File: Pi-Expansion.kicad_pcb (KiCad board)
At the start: 2 copper layers, 56 x 65 mm, 130 parts, among them J1 RPi_GPIO, J2 MMCX_H, J3 PINHEADER_2X2_SMD, P1 BATT, Q1 Q_NPN_BCE, U1 A2200-A, U2 SPX2920U-5.0

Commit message: made minor mods to power supply including moving reverse protection diode from negitive side to positive side to reduce voltage drop.
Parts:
- F1: value FUSE -> POLYFUSE
- U2: value SPX2920U-5.0 -> Racom R-78B5.0-1.5L
- moved D1 14.3 mm to (93.5, 128.5)
- moved D2 4.40 mm to (96.0, 128.5)
- moved U2 3.22 mm to (94.8, 125.2)
- moved F1 3.20 mm to (104.5, 120.5), turned to 0 degrees
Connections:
- D1 pad A: GND -> Net-(D1-PadA)
- F1 pad 1: Net-(F1-Pad1) -> GND
- P1 pad 1: Net-(D1-PadK) -> Net-(F1-Pad2)
- P1 pad 2: Net-(F1-Pad1) -> Net-(D1-PadA)
- U1 pad 23: GND -> (no net)
- U1 pad 24: GND -> (no net)
- U1 pad 25: GND -> (no net)
- U1 pad 26: GND -> (no net)
- U1 pad 27: GND -> (no net)
- U1 pad 29: GND -> (no net)
- U1 pad 30: GND -> (no net)
- U1 pad 31: GND -> (no net)
- U1 pad 32: GND -> (no net)
- U2 pad 1: Net-(F1-Pad2) -> Net-(D1-PadK)
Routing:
- net GND: track 78.3 -> 46.7 mm, vias 1 -> 3
- net Net-(D1-PadA): track 0.00 -> 12.9 mm
- net Net-(F1-Pad1): track 9.34 -> 0.00 mm
- net +5V: track 131.6 -> 135.3 mm
- net Net-(D1-PadK): track 2.52 -> 5.43 mm

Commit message: minor tweaks to in fill
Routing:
- net Net-(J2-Pad2): track 19.7 -> 1.47 mm
- added copper zone on F.Cu, net Net-(J2-Pad2)
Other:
- board text added: "2K2"
- board text removed: "GPLv3"
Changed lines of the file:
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@@
     (area 67.819999 72.349999 124.320001 137.850001)
     (thickness 1.6)
-    (drawings 26)
-    (tracks 331)
+    (drawings 25)
+    (tracks 321)
     (zones 0)
     (modules 130)
@@
     (effects (font (size 1 1) (thickness 0.25)))
   )
-  (gr_text 10K (at 80.75 122.25) (layer F.SilkS)
+  (gr_text 2K2 (at 80.75 122.25) (layer F.SilkS)
     (effects (font (size 1 1) (thickness 0.25)))
   )
@@
     (effects (font (size 1.5 1.5) (thickness 0.3)))
   )
-  (gr_text GPLv3 (at 112.25 83.75 90) (layer F.SilkS)
-    (effects (font (size 1.5 1.5) (thickness 0.3)))
-  )
   (gr_text 3.3v (at 93.7 108.9) (layer F.SilkS)
     (effects (font (size 1.5 1.5) (thickness 0.3)))
@@
   (gr_arc (start 71.57 76.1) (end 68.07 76.1) (angle 90) (layer Edge.Cuts) (width 0.5))
   (gr_arc (start 71.57 134.1) (end 71.57 137.6) (angle 90) (layer Edge.Cuts) (width 0.5))
-  (segment (start 103.75 125) (end 103.75 124.89808) (width 0.25) (layer F.Cu) (net 0))
   (segment (start 81.89 105.5) (end 76.25 105.5) (width 0.5) (layer B.Cu) (net 1))
   (segment (start 76.25 105.5) (end 72.84 108.91) (width 0.5) (layer B.Cu) (net 1))
@@
   (segment (start 79 97.42) (end 79 99.96) (width 0.5) (layer B.Cu) (net 9))
   (segment (start 79 99.96) (end 79 102.5) (width 0.5) (layer B.Cu) (net 9))
-  (segment (start 112.24 132.33) (end 112.24 130.76) (width 0.25) (layer F.Cu) (net 10) (status 10))
-  (segment (start 112.75 128.25) (end 111.95 127.45) (width 0.25) (layer F.Cu) (net 10) (status 20))
-  (segment (start 112.75 130.25) (end 112.75 128.25) (width 0.25) (layer F.Cu) (net 10))
-  (segment (start 112.24 130.76) (end 112.75 130.25) (width 0.25) (layer F.Cu) (net 10))
   (segment (start 111.95 127.45) (end 110.55 127.45) (width 0.25) (layer F.Cu) (net 10) (status 30))
-  (segment (start 110.55 127.45) (end 109.75 128.25) (width 0.25) (layer F.Cu) (net 10) (status 10))
-  (segment (start 109.75 128.25) (end 109.75 132.28) (width 0.25) (layer F.Cu) (net 10) (status 20))
   (segment (start 109.75 132.28) (end 109.7 132.33) (width 0.25) (layer F.Cu) (net 10) (status 30))
-  (segment (start 109.7 132.33) (end 109.7 134.87) (width 0.25) (layer F.Cu) (net 10) (status 30))
-  (segment (start 109.7 134.87) (end 112.24 134.87) (width 0.25) (layer F.Cu) (net 10) (status 30))
-  (segment (start 112.24 134.87) (end 112.24 132.33) (width 0.25) (layer F.Cu) (net 10) (status 30))
   (segment (start 111.15 128.72) (end 111.15 130.88) (width 0.25) (layer F.Cu) (net 11) (status 10))
   (segment (start 110.97 131.06) (end 110.97 133.6) (width 0.25) (layer F.Cu) (net 11) (status 20))
@@
       )
     )
+  )
+  (zone (net 10) (net_name "Net-(J2-Pad2)") (layer F.Cu) (hatch edge 0.508)
+    (priority 3)
+    (connect_pads yes (clearance 0.24))
+    (min_thickness 0.254)
+    (fill yes (arc_segments 16) (thermal_gap 0.508) (thermal_bridge_width 0.508) (smoothing chamfer))
+    (polygon
+      (pts
+        (xy 108.75 127) (xy 113.25 127) (xy 113.25 136) (xy 108.75 136) (xy 108.75 127.25)
+      )
+    )

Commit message: cleared out fabrication files as they should be generated fresh when needed, also simplified circuitry for the tx sense led
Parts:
- removed Q1: Q_NPN_BCE, TO_SOT_Packages_SMD:SOT-23
- removed R5: 2.2, Sailbot_Custom:Resistor-1206
- R2: value 10k -> 2.2K
- turned LED5 to 90 degrees
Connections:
- LED5 pad A: Net-(LED5-PadA) -> +3V3
- LED5 pad K: Net-(LED1-PadK) -> GPS_TX
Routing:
- net +3V3: track 164.1 -> 143.7 mm, vias 3 -> 0
- net GPS_TX: track 54.9 -> 64.9 mm, vias 2 -> 4
- net Net-(LED5-PadA): track 6.37 -> 0.00 mm
- net GND: track 46.7 -> 42.0 mm, vias 3 -> 1
- net Net-(Q1-Pad1): track 2.19 -> 0.00 mm
- net Net-(LED1-PadK): track 21.1 -> 19.1 mm

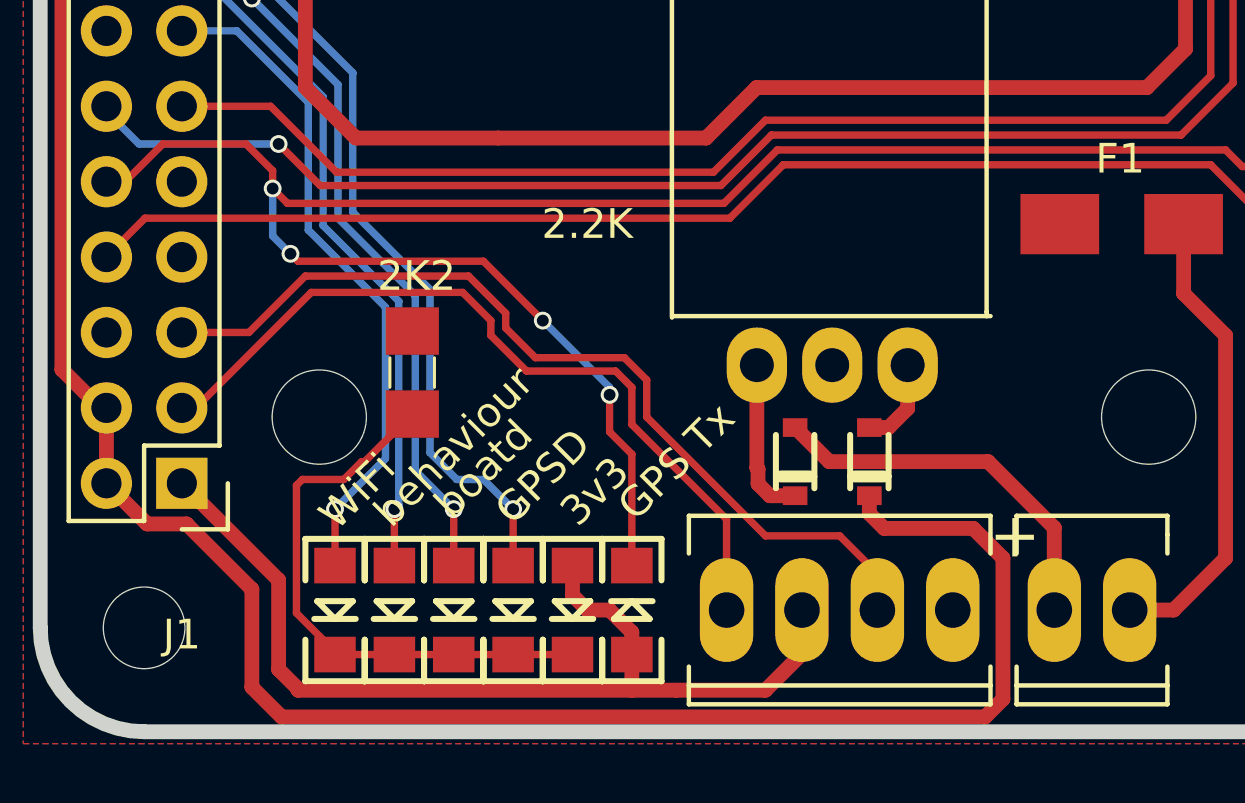
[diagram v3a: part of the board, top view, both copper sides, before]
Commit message: Added current limiting resistor for GPS TX indicator, also fiddled with Copper fill
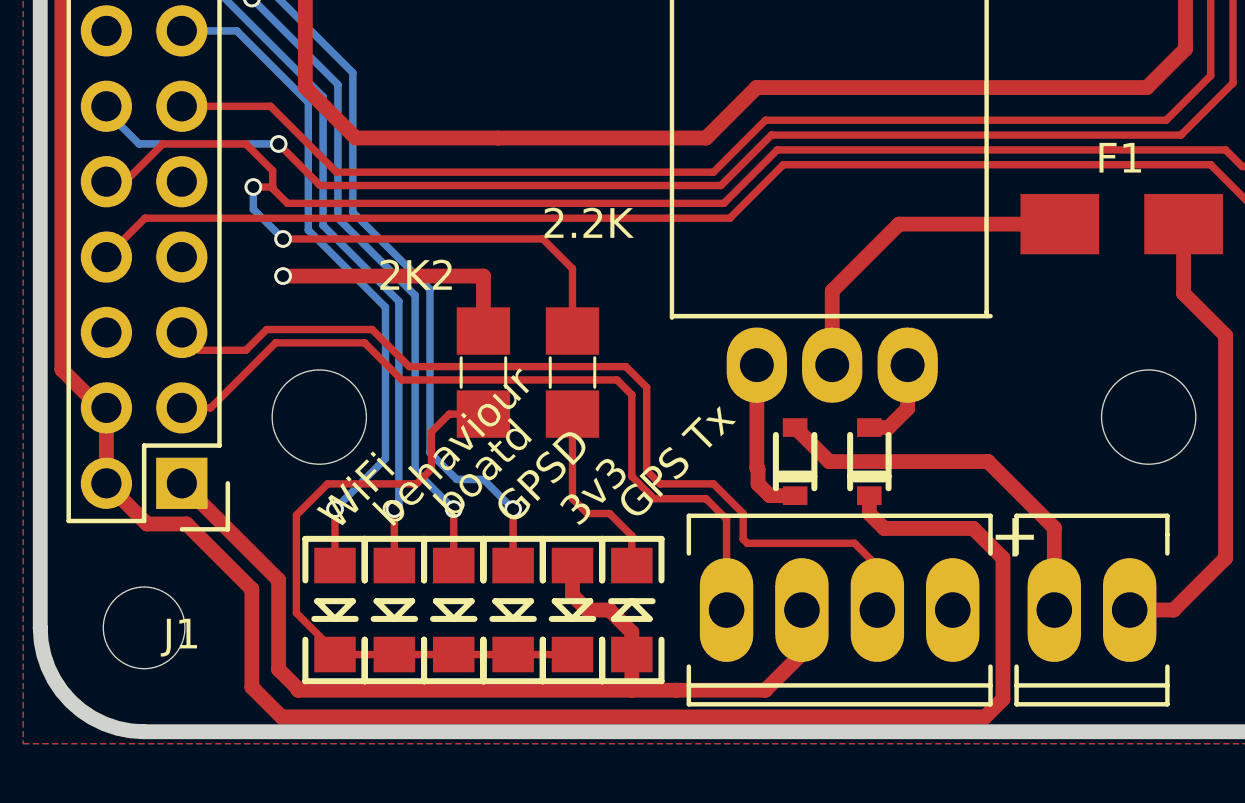
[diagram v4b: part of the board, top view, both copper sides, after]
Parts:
- added R5: 2.2K, FT:1206, F.Cu at (86.0, 125.5)
- moved R2 2.40 mm to (83.0, 125.5)
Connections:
- LED5 pad K: GPS_TX -> Net-(LED5-PadK)
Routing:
- net GND: track 42.0 -> 61.7 mm, vias 1 -> 2
- net Net-(LED5-PadK): track 0.00 -> 6.37 mm
- net GPS_TX: track 64.9 -> 58.7 mm, vias 4 -> 2
- net Net-(LED1-PadK): track 19.1 -> 21.7 mm
- net Net-(J1-Pad5): track 30.6 -> 32.1 mm
- added copper zone on F.Cu, net (none)
- removed copper zone on F.Cu, net GND

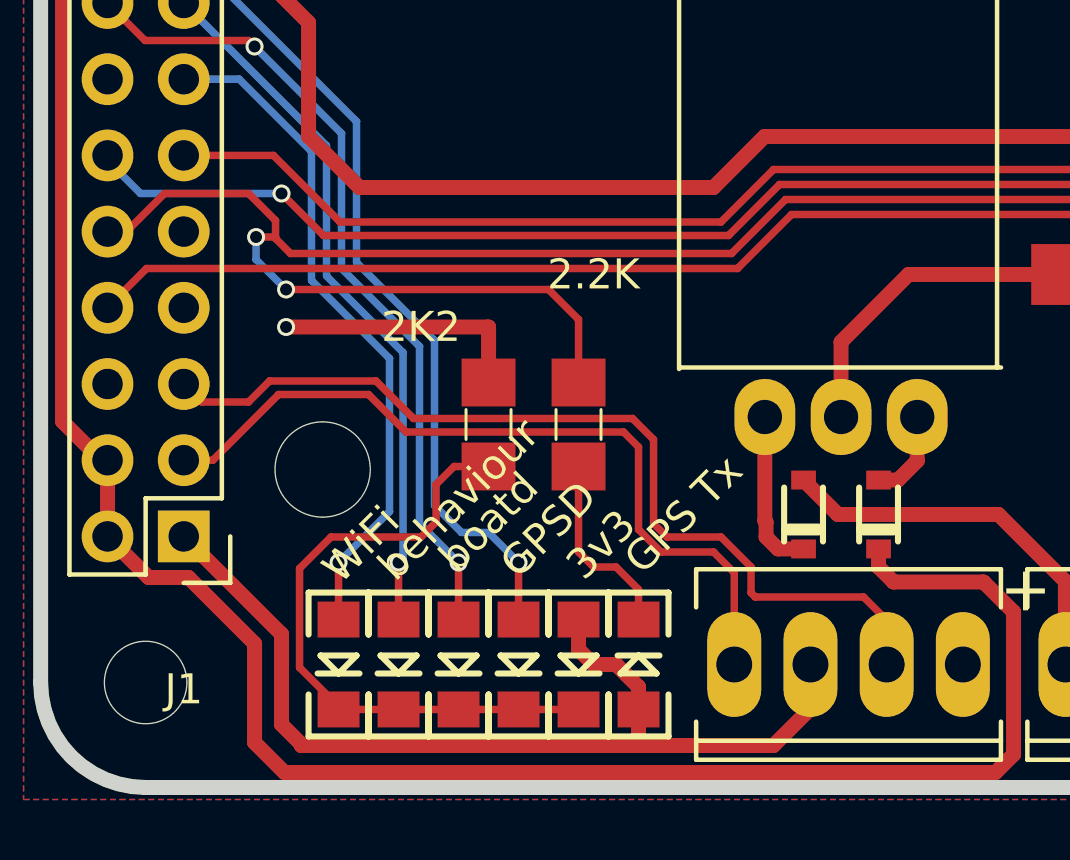
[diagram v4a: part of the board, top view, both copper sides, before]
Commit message: updated led resistor placement so they no longer obstruct the legand on the silk screen
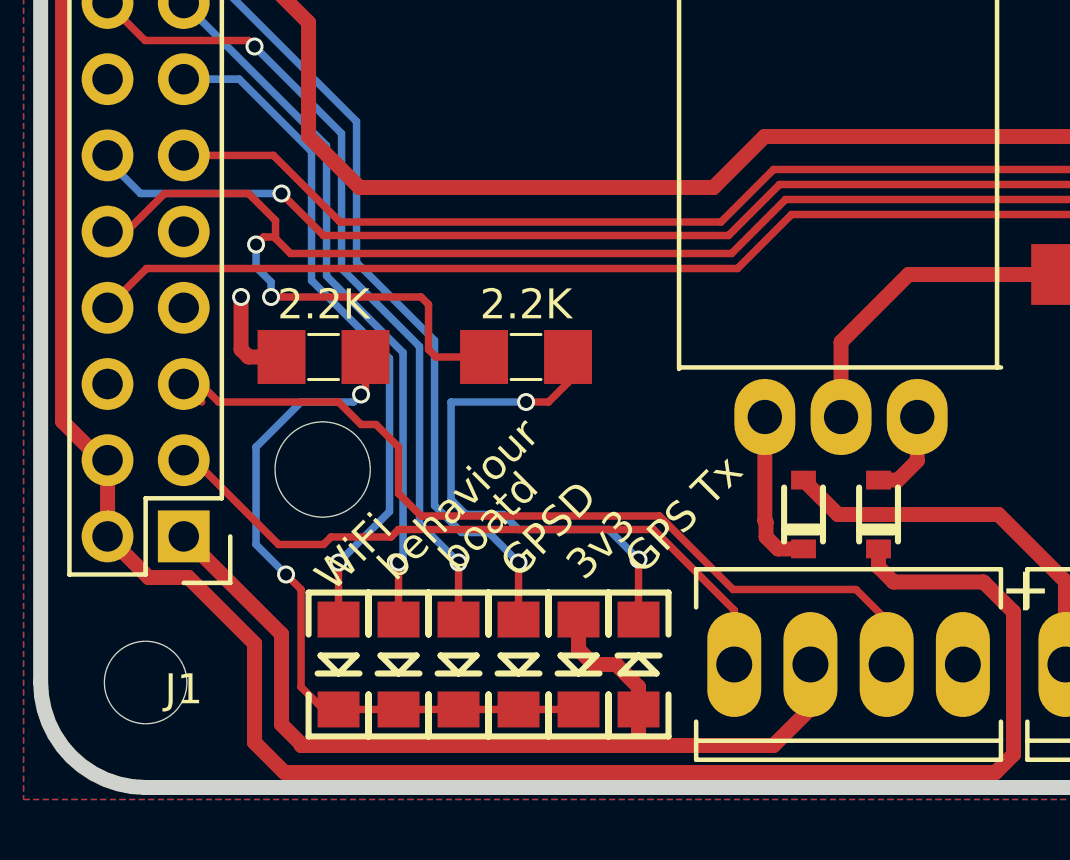
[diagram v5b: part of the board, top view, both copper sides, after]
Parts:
- moved R2 5.94 mm to (77.5, 123.2), turned to 180 degrees
- moved R5 2.85 mm to (84.2, 123.2), turned to 0 degrees
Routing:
- net Net-(LED5-PadK): track 6.37 -> 17.3 mm, vias 0 -> 2
- net GND: track 61.7 -> 56.3 mm
- net GPS_TX: track 58.7 -> 54.9 mm
- net Net-(J1-Pad3): track 26.9 -> 23.1 mm
- net Net-(LED1-PadK): track 21.7 -> 23.8 mm, vias 0 -> 2
- net Net-(J1-Pad5): track 32.1 -> 32.6 mm
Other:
- board text removed: "2K2"

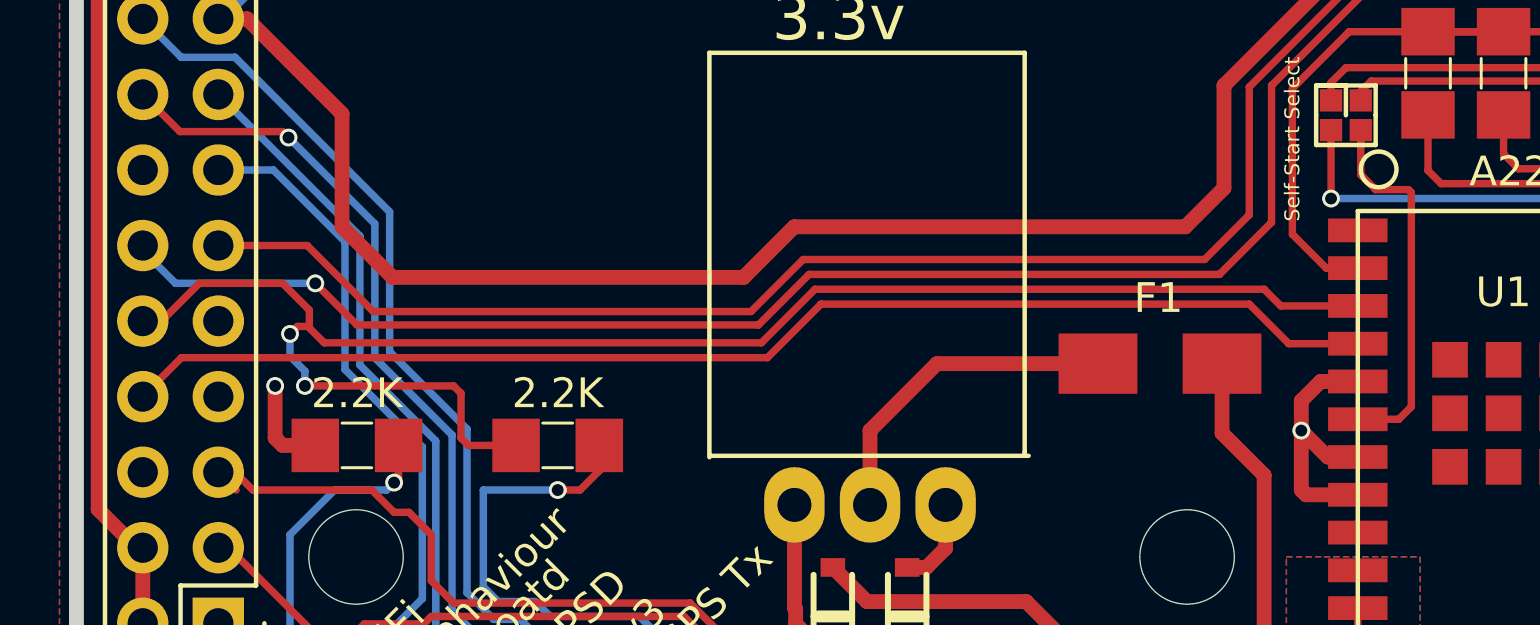
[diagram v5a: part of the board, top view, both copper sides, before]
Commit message: Final version sent to fab, retraced GPS_TX to fix net issue between 2k2 resistor and pi header
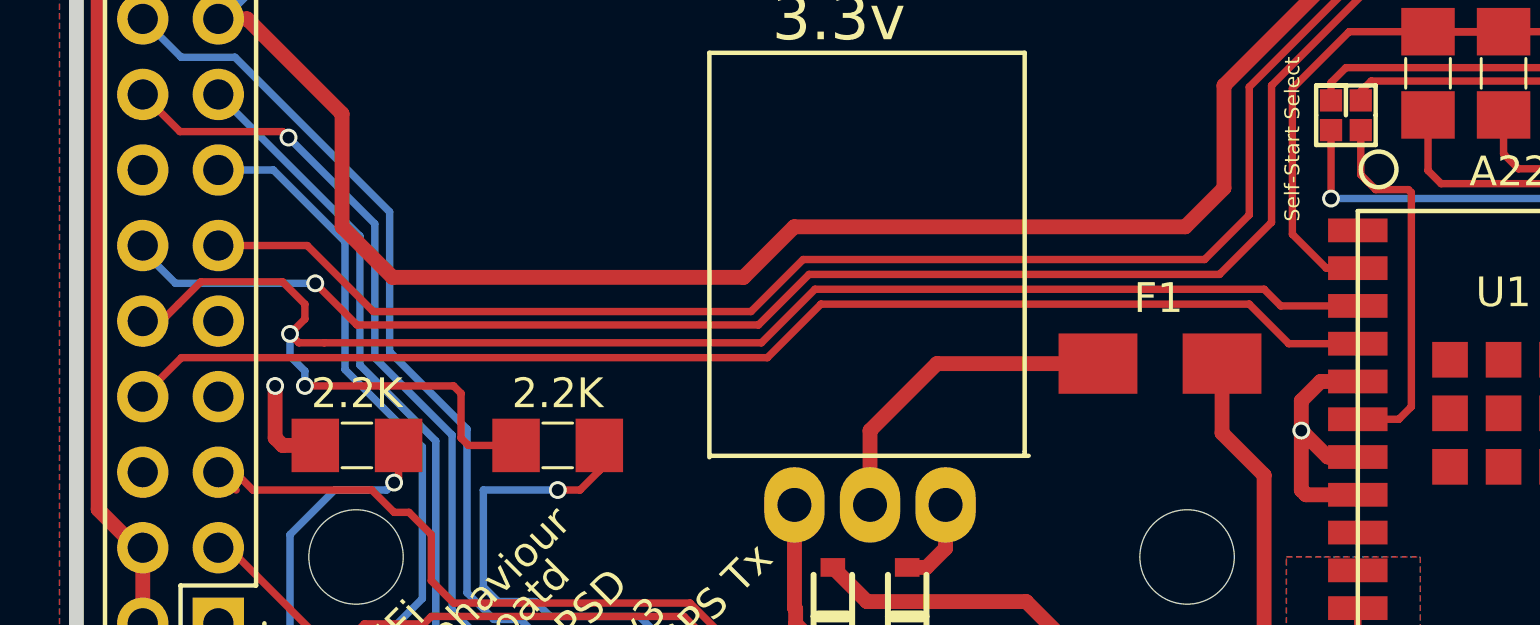
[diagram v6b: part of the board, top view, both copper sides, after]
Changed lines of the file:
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@@
   (general
     (links 86)
-    (no_connects 2)
-    (area 67.819999 72.349999 124.320001 137.850001)
+    (no_connects 1)
+    (area 67.5 56.852029 137.75 144.700001)
     (thickness 1.6)
     (drawings 25)
-    (tracks 328)
+    (tracks 329)
     (zones 0)
     (modules 129)
@@
   (layers
     (0 F.Cu signal)
-    (31 B.Cu power)
+    (31 B.Cu power hide)
     (32 B.Adhes user)
     (33 F.Adhes user)
@@
   (segment (start 107.5 118.5) (end 108.83 119.83) (width 0.25) (layer F.Cu) (net 4))
   (segment (start 70.3 121.61) (end 70.3 121.6) (width 0.25) (layer F.Cu) (net 4) (status 30))
+  (segment (start 70.3 119.07) (end 70.93 119.07) (width 0.25) (layer F.Cu) (net 5))
+  (segment (start 70.93 119.07) (end 71.5 118.5) (width 0.25) (layer F.Cu) (net 5))
+  (segment (start 76.4 119.8) (end 75.55 119.8) (width 0.25) (layer F.Cu) (net 5))
+  (segment (start 91.1 119.8) (end 76.4 119.8) (width 0.25) (layer F.Cu) (net 5))
+  (segment (start 108 118) (end 108.56 118.56) (width 0.25) (layer F.Cu) (net 5))
+  (segment (start 111.15 118.56) (end 108.56 118.56) (width 0.25) (layer F.Cu) (net 5) (status 20))
+  (segment (start 92.9 118) (end 91.1 119.8) (width 0.25) (layer F.Cu) (net 5))
+  (segment (start 92.9 118) (end 108 118) (width 0.25) (layer F.Cu) (net 5))
+  (segment (start 75.55 119.8) (end 75.25 119.5) (width 0.25) (layer F.Cu) (net 5))
+  (segment (start 75.25 119.5) (end 75.75 119) (width 0.25) (layer F.Cu) (net 5))
+  (segment (start 75.75 119) (end 75.75 118.5) (width 0.25) (layer F.Cu) (net 5))
+  (segment (start 75.75 118.5) (end 75 117.75) (width 0.25) (layer F.Cu) (net 5))
+  (segment (start 75 117.75) (end 72.25 117.75) (width 0.25) (layer F.Cu) (net 5))
+  (segment (start 72.25 117.75) (end 71.5 118.5) (width 0.25) (layer F.Cu) (net 5))
   (segment (start 82.85046 123.25) (end 81.25 123.25) (width 0.25) (layer F.Cu) (net 5))
-  (segment (start 75.5 119.25) (end 75.75 119.25) (width 0.25) (layer F.Cu) (net 5))
-  (segment (start 75.25 119.5) (end 75.5 119.25) (width 0.25) (layer F.Cu) (net 5))
   (via (at 75.25 119.5) (size 0.6) (drill 0.4) (layers F.Cu B.Cu) (net 5))
   (segment (start 75.25 120.25) (end 75.25 119.5) (width 0.25) (layer B.Cu) (net 5))
@@
   (segment (start 81 123) (end 81 121.5) (width 0.25) (layer F.Cu) (net 5))
   (segment (start 81.25 123.25) (end 81 123) (width 0.25) (layer F.Cu) (net 5))
-  (segment (start 92.9 118) (end 108 118) (width 0.25) (layer F.Cu) (net 5))
-  (segment (start 92.9 118) (end 91.1 119.8) (width 0.25) (layer F.Cu) (net 5))
-  (segment (start 108.56 118.56) (end 111.15 118.56) (width 0.25) (layer F.Cu) (net 5) (status 20))
-  (segment (start 108 118) (end 108.56 118.56) (width 0.25) (layer F.Cu) (net 5))
-  (segment (start 75.9 119.3) (end 75.9 118.7) (width 0.25) (layer F.Cu) (net 5))
-  (segment (start 72.2 117.8) (end 70.93 119.07) (width 0.25) (layer F.Cu) (net 5) (status 20))
-  (segment (start 72.2 117.8) (end 75 117.8) (width 0.25) (layer F.Cu) (net 5))
-  (segment (start 75.9 118.7) (end 75 117.8) (width 0.25) (layer F.Cu) (net 5))
-  (segment (start 70.3 119.07) (end 70.93 119.07) (width 0.25) (layer F.Cu) (net 5) (status 30))
-  (segment (start 75.9 119.3) (end 76.4 119.8) (width 0.25) (layer F.Cu) (net 5))
-  (segment (start 91.1 119.8) (end 76.4 119.8) (width 0.25) (layer F.Cu) (net 5))
   (segment (start 80 132.0014) (end 80 130.1) (width 0.25) (layer F.Cu) (net 6) (status 10))
   (segment (start 72.84 111.45) (end 77.6 116.21) (width 0.25) (layer B.Cu) (net 6) (status 10))
